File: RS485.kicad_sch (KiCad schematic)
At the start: 9 parts, among them J5 RJ45, J6 RJ45, U1 ST485E

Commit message: wip
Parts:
- removed R19: 120, Resistor_SMD:R_0805_2012Metric, symbol Device:R
- removed U6: ~, symbol FOC:PI121
- added IC1: 131M61, 131M61:SOIC127P1030X265-16N, symbol PI_131:131M61
- J5, J6: footprint Connector_RJ:RJ45_Amphenol_54602-x08_Horizontal -> Connector_RJ:RJ45_OST_PJ012-8P8CX_Vertical
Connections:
- net +3.3V: now also C15.2, IC1.1 (VDD1), IC1.7 (EN1); no longer C16.1
- net GNDD: now also C15.1, IC1.2 (GND1_1), IC1.8 (GND1_2)
- net GNDS: now also C16.2, IC1.15 (GND2_2), IC1.9 (GND2_1); no longer C15.1
- net RS485_Rx: now also IC1.5 (VOC)
- net RS485_Tx: now also IC1.4 (VIB)
- net at U1.1 (RO): now also IC1.12 (VIC); no longer R8.1
- net at U1.2 (~{RE}): now also U1.3 (DE), IC1.14 (VOA); no longer R8.2
- net at U1.4 (DI): now also IC1.13 (VOB)
- net at U1.6 (A): now also R8.2
- net at U1.7 (B): now also R8.1
- new net: IC1.10 (EN2), IC1.16 (VDD2)
- new net RS485_DE: IC1.3 (VIA)
- no-connect marks 0 -> 2
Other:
- note removed: "pi121 or pi122"
- moved on the sheet: C11, R8, U1

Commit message: wip
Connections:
- net GNDS: no longer IC1.15 (GND2_2), IC1.9 (GND2_1), U1.5 (GND)
- net VCC_ISO: now reaches J6.1
- net VCC_ISO: now also C11.2, C16.1, IC1.10 (EN2), IC1.16 (VDD2), J5.1, J5.2, J5.3, J6.2, J6.3, U1.8 (VCC)
- net at J6.4: now also J5.4, R8.1, U1.7 (B)
- net at J6.5: now also J5.5, R8.2, U1.6 (A)
- net GND_ISO: now reaches J6.6
- net GND_ISO: now also IC1.15 (GND2_2), IC1.9 (GND2_1), J5.6, J5.7, J5.8, J6.7, J6.8, U1.5 (GND)
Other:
- note added: "ESD?"
- note added: "Galvanic Isolation"
- moved on the sheet: C11, C15, J5, J6, R8, U1

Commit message: 90% schematic first layout
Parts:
- J6: footprint Connector_RJ:RJ45_OST_PJ012-8P8CX_Vertical -> Connector_RJ:RJ45_Amphenol_54602-x08_Horizontal
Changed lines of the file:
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@@
 			)
 		)
-		(property "Footprint" "Connector_RJ:RJ45_OST_PJ012-8P8CX_Vertical"
+		(property "Footprint" "Connector_RJ:RJ45_Amphenol_54602-x08_Horizontal"
 			(at 34.925 77.47 90)
 			(effects

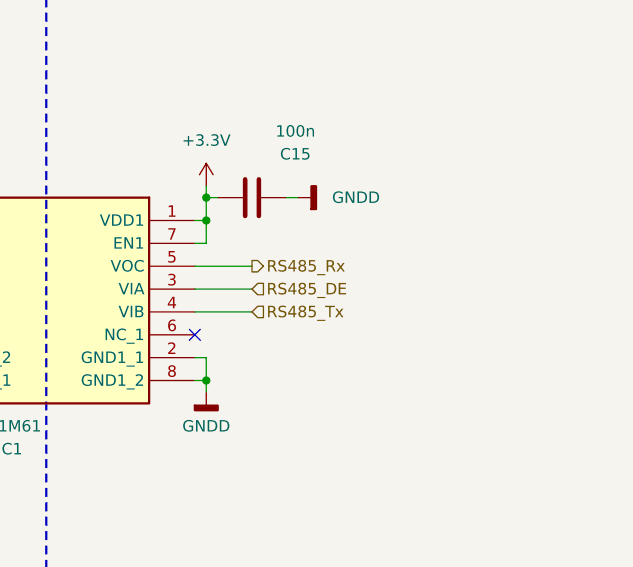
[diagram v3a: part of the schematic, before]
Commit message: Addition of testpoints
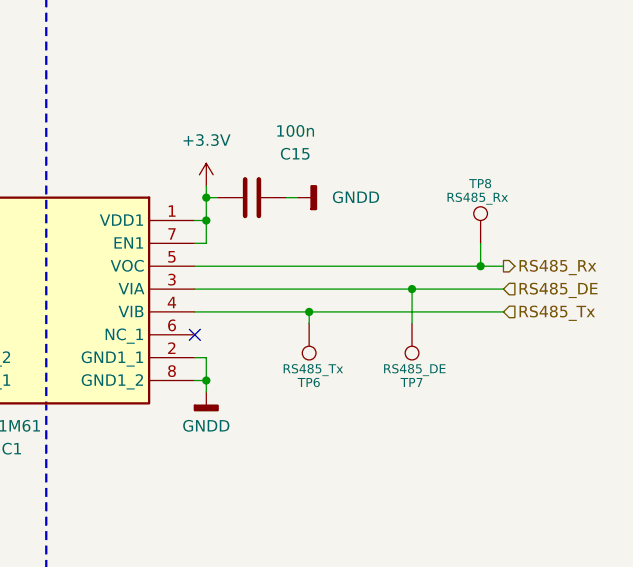
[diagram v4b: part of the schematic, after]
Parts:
- added TP6: RS485_Tx, TestPoint:TestPoint_Pad_D1.0mm, symbol Connector:TestPoint
- added TP7: RS485_DE, TestPoint:TestPoint_Pad_D1.0mm, symbol Connector:TestPoint
- added TP8: RS485_Rx, TestPoint:TestPoint_Pad_D1.0mm, symbol Connector:TestPoint
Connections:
- net RS485_DE: now also TP7.1
- net RS485_Rx: now also TP8.1
- net RS485_Tx: now also TP6.1
